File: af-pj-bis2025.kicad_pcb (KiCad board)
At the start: 2 copper layers, 180 x 105.5 mm, 72 parts, among them U1 MIC5237-5.0YU, U2 ALD114904APAL, U3 OPA2380AIDGKR, U4 THS4552IPWR, U5 REF5050IDR, U6 LT1991ACMS-TRPBF, U7 UA78L06ACPK, U8 ADS1220IPW

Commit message: 差動増幅回路のレイアウト完了
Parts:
- added H1: MountingHole, MountingHole:MountingHole_3.2mm_M3, F.Cu at (17.8, 3.48)
- added H1: MountingHole, MountingHole:MountingHole_3.2mm_M3, F.Cu at (65.1, 141.1)
- added H2: MountingHole, MountingHole:MountingHole_3.2mm_M3, F.Cu at (32.1, 89.1)
- added H2: MountingHole, MountingHole:MountingHole_3.2mm_M3, F.Cu at (17.8, 11.4)
- added H3: MountingHole, MountingHole:MountingHole_3.2mm_M3, F.Cu at (17.8, 19.4)
- added H3: MountingHole, MountingHole:MountingHole_3.2mm_M3, F.Cu at (80.4, 90.4)
- added J1: CN7, Connector_PinSocket_2.54mm:PinSocket_2x19_P2.54mm_Vertical, F.Cu at (4.37, 1.82)
- added J1: CN7, Connector_PinSocket_2.54mm:PinSocket_2x19_P2.54mm_Vertical, B.Cu at (24.5, 92.9)
- added J2: CN10, Connector_PinSocket_2.54mm:PinSocket_2x19_P2.54mm_Vertical, F.Cu at (11.5, 1.82)
- added J2: CN10, Connector_PinSocket_2.54mm:PinSocket_2x19_P2.54mm_Vertical, B.Cu at (85.5, 92.9)
- added J3: Conn_01x06, Connector_PinSocket_2.54mm:PinSocket_1x06_P2.54mm_Vertical, F.Cu at (374.5, 161.4)
- added J4: Conn_Coaxial, Connector_Coaxial:SMA_Amphenol_901-143_Horizontal, F.Cu at (154.0, 113.8)
- added J5: Barrel_Jack_MountingPin, Connector_BarrelJack:BarrelJack_Horizontal, F.Cu at (112.0, 115.8)
- added J7: Conn_Coaxial, Connector_Coaxial:SMA_Amphenol_901-143_Horizontal, F.Cu at (134.2, 113.8)
- C1: footprint pj-bis2025:tantal_TAJR105K016RNJ_TAJR_AVX-M -> pj-bis2025:LDO_5V_out_TAJR105K016RNJAC_TAJR_AVX
- moved C22 291.6 mm to (386.0, 245.5), turned to 90 degrees
- moved C15 286.6 mm to (386.0, 230.2), turned to 90 degrees
- moved C11 279.7 mm to (372.0, 228.8), turned to 180 degrees
- moved C24 277.5 mm to (372.0, 247.2), turned to 180 degrees
- moved C18 276.7 mm to (372.0, 244.0), turned to 180 degrees
- moved C17 272.2 mm to (372.0, 232.0), turned to 180 degrees
- moved C21 271.8 mm to (360.0, 245.7), turned to 90 degrees
- moved C12 271.5 mm to (360.0, 235.2)
- moved C19 271.4 mm to (360.0, 239.0)
- moved Re19 270.8 mm to (382.8, 244.3)
- moved Re9 269.7 mm to (382.8, 229.0)
- moved Re18 268.9 mm to (378.5, 244.3)
- moved Re21 268.9 mm to (382.8, 246.8)
- moved C20 268.4 mm to (353.5, 245.7), turned to 90 degrees
- moved Re11 267.9 mm to (382.8, 231.5)
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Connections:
- net Net-(C13-Pad1) renamed /diff1_in_N
- net Net-(C13-Pad2) renamed /diff1_in_P
- net Net-(C20-Pad1) renamed /diff3_in_N
- net Net-(C20-Pad2) renamed /diff3_in_P
- net Net-(Re10-Pad2) renamed /diff2_out_P
- net Net-(Re15-Pad2) renamed /diff4_out_N
- net Net-(Re20-Pad2) renamed /diff4_out_P
- net Net-(Re5-Pad2) renamed /diff2_out_N
- net Net-(U4A-VIN1+) renamed /diff2_in_P
- net Net-(U4A-VIN1-) renamed /diff2_in_N
- net Net-(U4A-VOUT1+) renamed /diff1_out_P
- net Net-(U4A-VOUT1-) renamed /diff1_out_N
- net Net-(U4B-VIN2+) renamed /diff4_in_P
- net Net-(U4B-VIN2-) renamed /diff4_in_N
- net Net-(U4B-VOUT2+) renamed /diff3_out_P
- net Net-(U4B-VOUT2-) renamed /diff3_out_N
- C15 pad 1: /AIN1P -> /AIN1P_in+
- C15 pad 2: /AIN1N -> /AIN1N_in-
- Re11 pad 2: /AIN1P -> /AIN1P_in+
- Re9 pad 2: /AIN1N -> /AIN1N_in-
- U8 pad 10: /AIN1N -> /AIN1N_adc
- U8 pad 11: /AIN1P -> /AIN1P_adc
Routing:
- net /DC_9V: track 0.00 -> 32.8 mm
- net /diff2_in_P: track 0.00 -> 27.2 mm, vias 0 -> 4
- net /diff4_in_N: track 0.00 -> 27.1 mm, vias 0 -> 4
- net /diff2_in_N: track 0.00 -> 25.5 mm, vias 0 -> 4
- net /diff4_in_P: track 0.00 -> 25.3 mm, vias 0 -> 4
- net /AVSS: track 0.00 -> 21.0 mm, vias 0 -> 1
- net /AVDD_5V: track 0.00 -> 19.9 mm, vias 0 -> 4
- net /AVDD_6.2V: track 0.00 -> 18.3 mm, vias 0 -> 2
- net /VREF_0.5V: track 0.00 -> 17.4 mm, vias 0 -> 2
- net /diff1_in_N: track 0.00 -> 16.8 mm, vias 0 -> 2
- net /diff1_in_P: track 0.00 -> 16.8 mm, vias 0 -> 2
- net /diff4_out_P: track 0.00 -> 16.5 mm, vias 0 -> 2
- net /diff2_out_P: track 0.00 -> 16.5 mm, vias 0 -> 2
- net /diff3_in_N: track 0.00 -> 16.4 mm, vias 0 -> 2
- net /diff3_in_P: track 0.00 -> 16.4 mm, vias 0 -> 2
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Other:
- board size 180 x 105.5 mm -> 250.2 x 105.5 mm

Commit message: AVSS接続完了
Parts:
- removed the H1 at (17.8, 3.48)
- removed the H2 at (17.8, 11.4)
- removed the H3 at (17.8, 19.4)
- removed the J1 at (4.37, 1.82)
- removed the J2 at (11.5, 1.82)
- moved Re28 180.9 mm to (215.8, 130.0), turned to -90 degrees
- moved Re27 178.7 mm to (218.2, 130.0), turned to 90 degrees
- moved Re29 175.7 mm to (220.8, 130.0), turned to 90 degrees
- moved Re21 174.8 mm to (242.5, 142.5), turned to -90 degrees
- moved Re22 174.5 mm to (242.2, 110.0), turned to -90 degrees
- moved Re20 174.0 mm to (242.5, 138.2), turned to -90 degrees
- moved C24 173.9 mm to (242.0, 131.7), turned to 90 degrees
- moved C22 173.7 mm to (243.8, 145.8), turned to 0 degrees
- moved Re24 173.6 mm to (242.0, 127.2), turned to -90 degrees
- moved Re23 173.6 mm to (242.2, 116.5), turned to -90 degrees
- moved C20 172.2 mm to (243.5, 113.2), turned to 0 degrees
- moved C32 172.0 mm to (225.7, 130.5), turned to 0 degrees
- moved C21 171.6 mm to (243.5, 119.8), turned to 0 degrees
- moved Re19 171.3 mm to (245.0, 142.5), turned to -90 degrees
- moved Re16 170.9 mm to (244.8, 110.0), turned to -90 degrees
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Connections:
- net /AIN1N_mcu renamed /AIN2_mcuN
- net /AIN1P_mcu renamed /AIN2_mcuP
- C15 pad 1: /AIN1P_in+ -> /AIN1P
- C15 pad 2: /AIN1N_in- -> /AIN1N
- C22 pad 1: /AIN2P -> /AIN2_inP
- C22 pad 2: /AIN2N -> /AIN2_inN
- C7 pad 2: /OUT1 -> /OUT2
- C9 pad 2: /OUT2 -> /OUT1
- J3 pad 2: /AIN1N_in -> /AIN2_inN
- J3 pad 3: /AIN1N_adc -> /AIN2_adcN
- J3 pad 4: /AIN1P_adc -> /AIN2_adcP
- J3 pad 5: /AIN1P_in -> /AIN2_inP
- J4 pad 1: /GATE2 -> /GATE1
- J7 pad 1: /GATE1 -> /GATE2
- Re1 pad 1: /OUT1 -> /OUT2
- Re11 pad 2: /AIN1P_in+ -> /AIN1P
- Re19 pad 2: /AIN2N -> /AIN2_inN
- Re2 pad 1: /OUT2 -> /OUT1
- Re21 pad 2: /AIN2P -> /AIN2_inP
- Re3 pad 2: /OUT1 -> /OUT2
- Re4 pad 2: /OUT2 -> /OUT1
- Re9 pad 2: /AIN1N_in- -> /AIN1N
- U2 pad 2: /GATE1 -> /GATE2
- U2 pad 7: /GATE2 -> /GATE1
- U8 pad 10: /AIN1N_adc -> /AIN1N
- U8 pad 11: /AIN1P_adc -> /AIN1P
- U8 pad 6: /AIN2N -> /AIN2_adcN
- U8 pad 7: /AIN2P -> /AIN2_adcP
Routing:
- net /AVSS: track 21.0 -> 125.9 mm, vias 1 -> 29
- net /AIN1N: track 0.00 -> 54.9 mm, vias 0 -> 2
- net /AIN1P: track 0.00 -> 54.2 mm, vias 0 -> 2
- net /VREF_5V: track 15.7 -> 45.0 mm, vias 0 -> 2
- net /AIN2_inP: track 0.00 -> 21.8 mm
- net /AIN2_inN: track 0.00 -> 16.6 mm
- net /AIN2_adcP: track 0.00 -> 15.5 mm
- net /AIN2_adcN: track 0.00 -> 15.4 mm
- net /OUT2: track 5.34 -> 17.4 mm
- net /VREF_0.5V: track 17.4 -> 27.7 mm
- net /OUT1: track 5.34 -> 14.4 mm
- net Net-(U8-DIN): track 0.00 -> 8.21 mm
- net /DVDD: track 0.00 -> 6.73 mm
- net Net-(U8-DOUT/*DRDY): track 0.00 -> 6.44 mm
- net Net-(U8-SCLK): track 0.00 -> 4.82 mm
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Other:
- board size 250.2 x 105.5 mm -> 250.8 x 105.5 mm

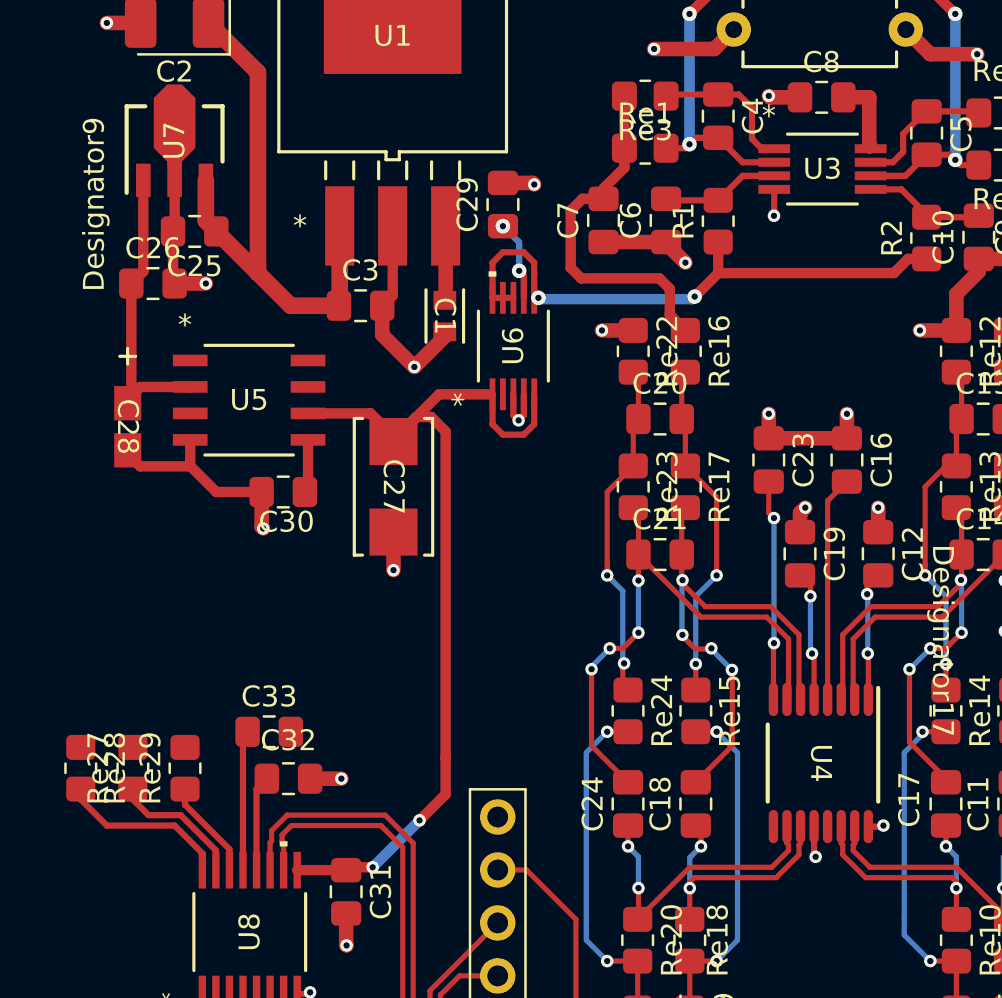
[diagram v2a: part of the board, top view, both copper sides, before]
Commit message: AVDD-5Vを配線
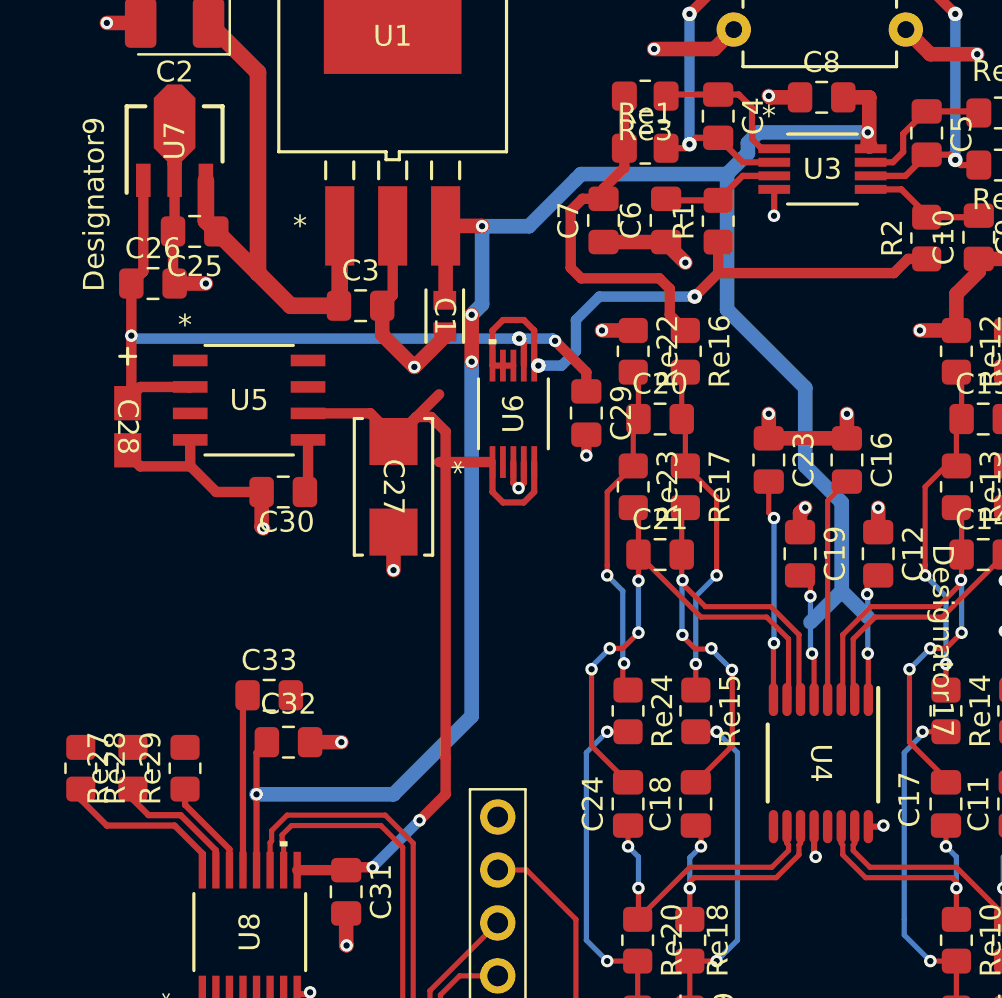
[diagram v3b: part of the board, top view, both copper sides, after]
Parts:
- moved C29 10.8 mm to (240.0, 113.0), turned to -90 degrees
- moved U6 3.25 mm to (236.5, 113.0)
- moved C32 1.75 mm to (225.7, 128.8)
- moved C33 1.75 mm to (224.8, 126.5)
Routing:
- net /AVDD_5V: track 24.5 -> 111.1 mm, vias 4 -> 9
- net /AVDD_6.2V: track 18.3 -> 39.3 mm, vias 2 -> 3
- net /VREF_0.5V: track 27.7 -> 29.9 mm
- net /DVDD: track 6.73 -> 8.48 mm
- net /AVSS: track 125.9 -> 125.3 mm

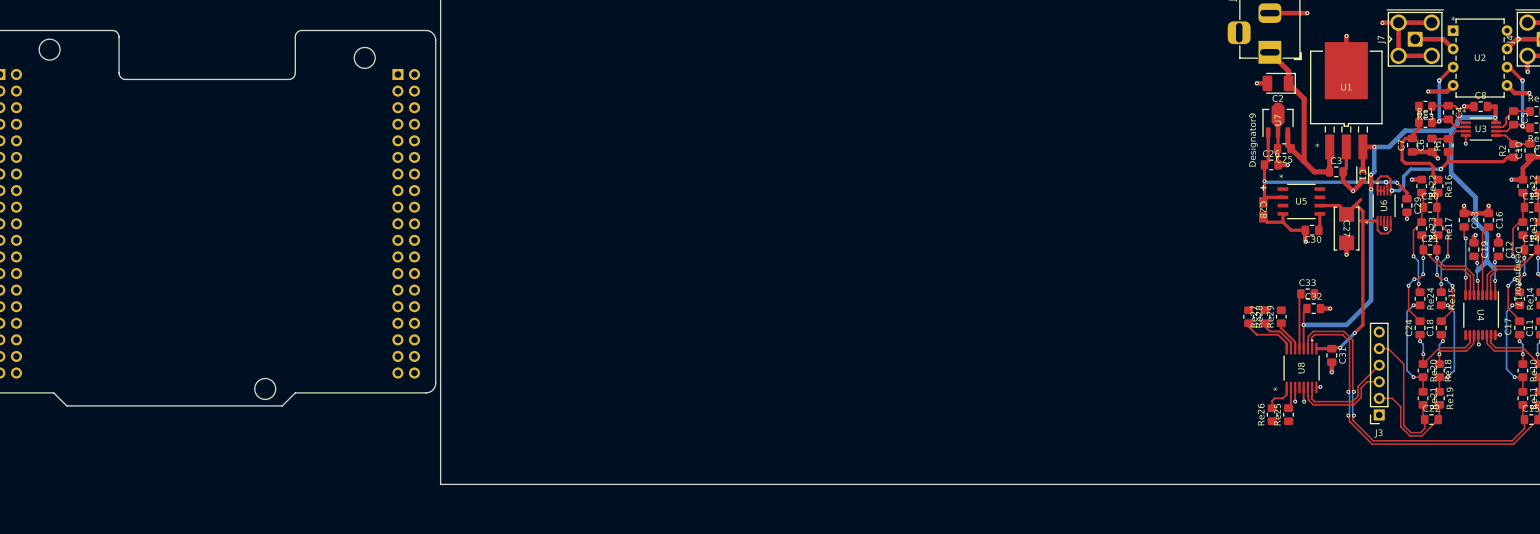
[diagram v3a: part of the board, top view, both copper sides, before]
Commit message: LCDの配線完了
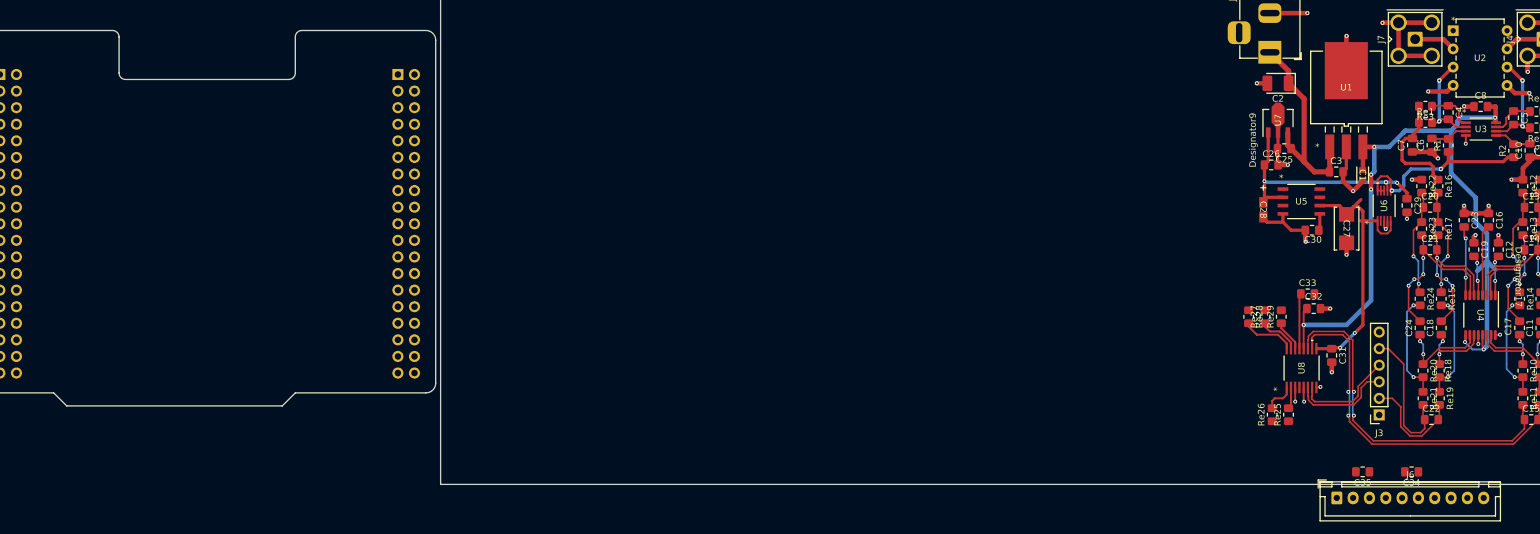
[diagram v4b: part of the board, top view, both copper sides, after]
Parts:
- removed H1, H2, H3: MountingHole, MountingHole:MountingHole_3.2mm_M3
- added C34: 0.1u, Capacitor_SMD:C_0805_2012Metric_Pad1.18x1.45mm_HandSolder, F.Cu at (240.7, 153.8)
- added C35: 0.1u, Capacitor_SMD:C_0805_2012Metric_Pad1.18x1.45mm_HandSolder, F.Cu at (233.2, 153.8)
- added J6: Conn_01x10, Connector_JST:JST_XH_B10B-XH-A_1x10_P2.50mm_Vertical, F.Cu at (229.2, 157.8)
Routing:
- net /AVDD_5V: track 111.1 -> 131.5 mm, vias 9 -> 11

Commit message: ADCのディジタル配線完了
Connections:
- net /CS* renamed /ADC_CS
- net /DIN renamed /ADC_MOSI
- net /DOUT renamed /ADC_MISO
- net /DRDY renamed /ADC_DRDY
- net /LCD_SCK renamed /LCD_SCLK
- net /SCLK renamed /ADC_SCLK

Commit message: EdgeCutsを調整した
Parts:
- removed J6: Conn_01x10, Connector_JST:JST_XH_B10B-XH-A_1x10_P2.50mm_Vertical
- added J8: Conn_01x10, Connector_JST:JST_XH_B10B-XH-A_1x10_P2.50mm_Vertical, F.Cu at (177.2, 132.8)
- moved J2 125.4 mm to (210.8, 88.2)
- moved J1 125.4 mm to (149.8, 88.2)
- moved C13 63.1 mm to (200.8, 89.1)
- moved C14 63.1 mm to (200.8, 95.6)
- moved C15 63.1 mm to (200.8, 121.6)
- moved C10 63.1 mm to (200.6, 80.4)
- moved C11 63.1 mm to (202.2, 107.5)
- moved C12 63.1 mm to (195.8, 95.5)
- moved C16 63.1 mm to (194.2, 91.0)
- moved C17 63.1 mm to (199.0, 107.5)
- moved C18 63.1 mm to (187.0, 107.5)
- moved C19 63.1 mm to (192.0, 95.5)
- moved C23 63.1 mm to (190.5, 91.0)
- moved C24 63.1 mm to (183.8, 107.5)
- moved C29 63.1 mm to (181.8, 88.8)
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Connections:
- C33 pad 1: /DVDD -> +3V3
- C33 pad 2: /DVSS -> /AVSS
- U8 pad 13: /DVDD -> +3V3
- U8 pad 4: /DVSS -> /AVSS
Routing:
- net +3V3: track 0.00 -> 17.5 mm
- net GND: track 0.00 -> 15.7 mm
- net /DVDD: track 8.48 -> 0.00 mm
- net /LCD_DISP: track 0.00 -> 4.00 mm
- net /VREF_5V: track 45.0 -> 41.6 mm
- net /AVSS: track 125.2 -> 123.6 mm, vias 29 -> 28
- added copper zone on B.Cu, net /AVSS
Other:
- board size 250.8 x 105.5 mm -> 70 x 88.8 mm
